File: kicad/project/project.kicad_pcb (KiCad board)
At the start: 2 copper layers, 98 x 60 mm, 49 parts, among them J1 SWD, J3 Voltmeter, U1 ADS1015, U2 AP7380, U3 STM32L031F4Px, U4 VN7003ALH

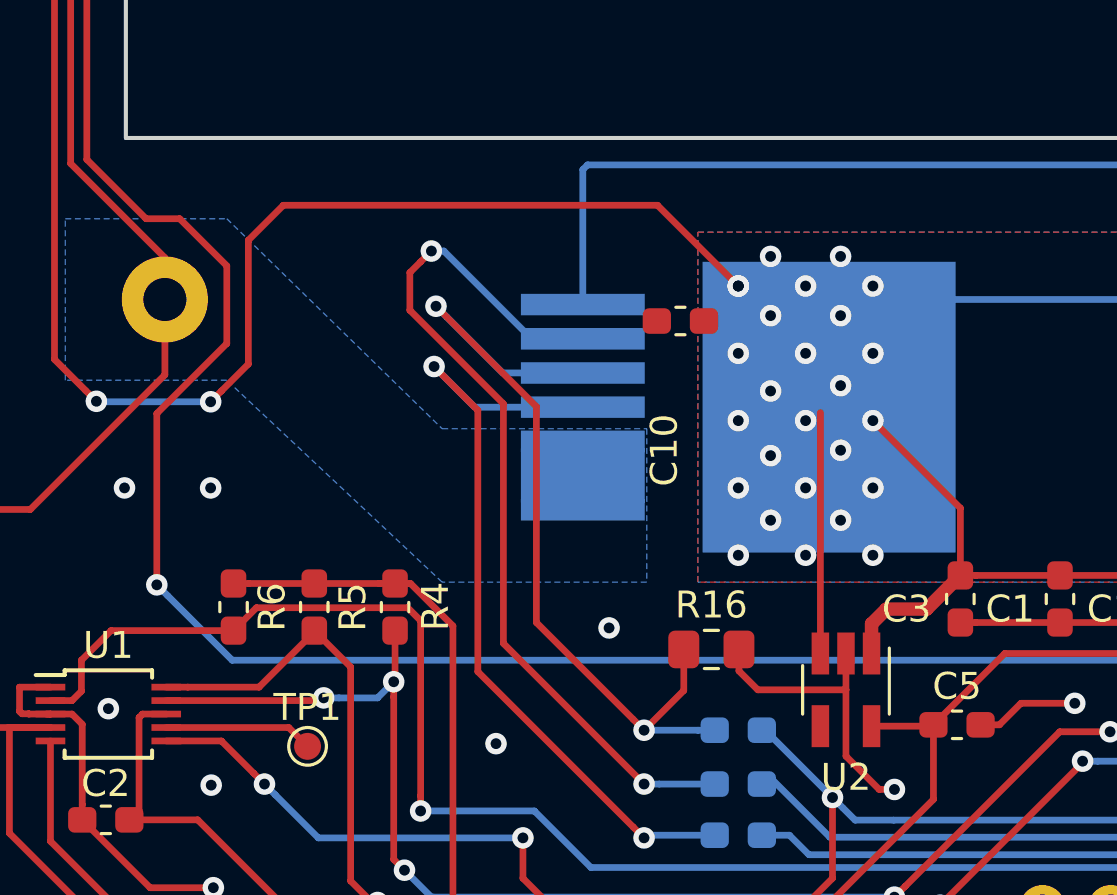
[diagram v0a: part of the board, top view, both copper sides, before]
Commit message: Corrected octopak footprint
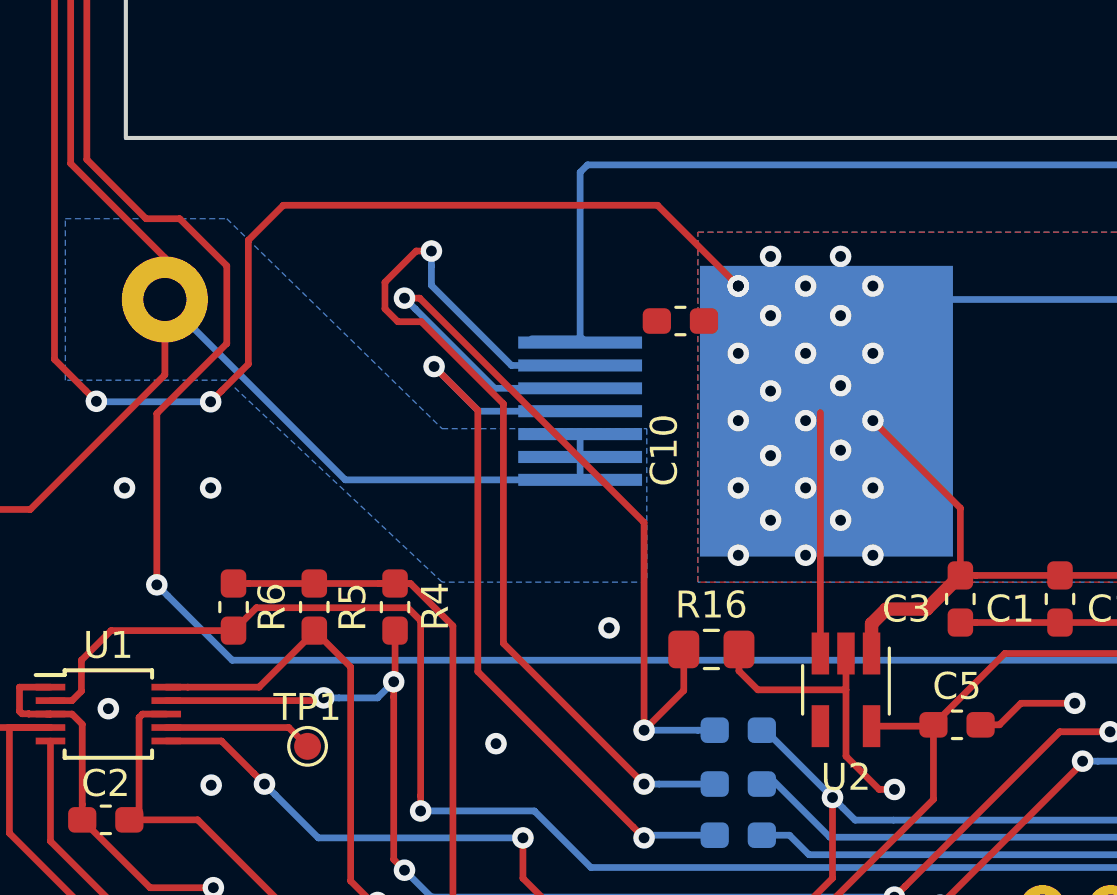
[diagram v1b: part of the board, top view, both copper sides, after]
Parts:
- moved U4 0.18 mm to (137.4, 112.2)
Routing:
- net /OUT: track 61.2 -> 81.1 mm
- net GND: track 178.3 -> 181.7 mm
- net /FR_DIAG: track 33.6 -> 36.2 mm
- net Net-(R13-Pad1): track 31.7 -> 34.2 mm

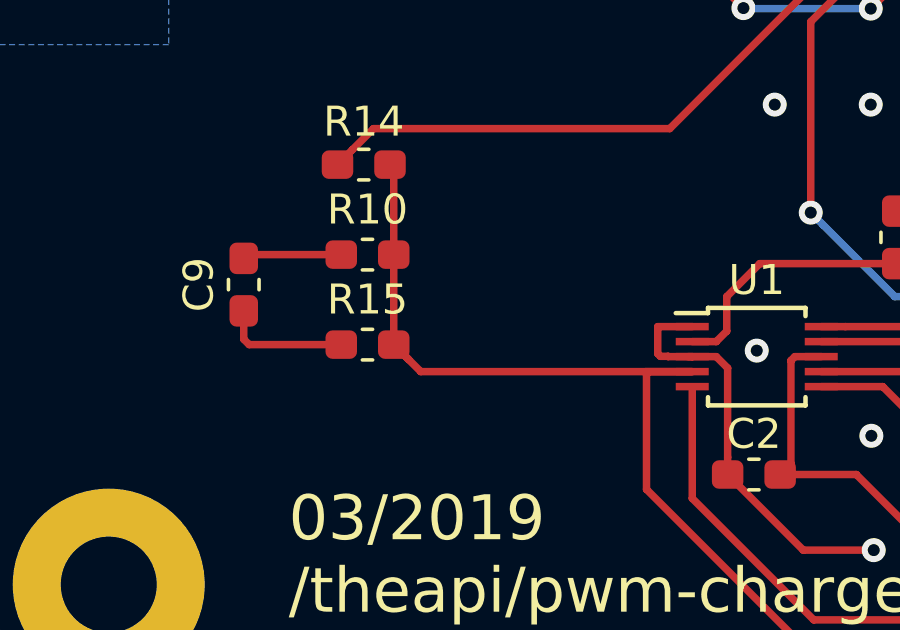
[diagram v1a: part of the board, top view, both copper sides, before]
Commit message: BATT_SENSE RC filter fix
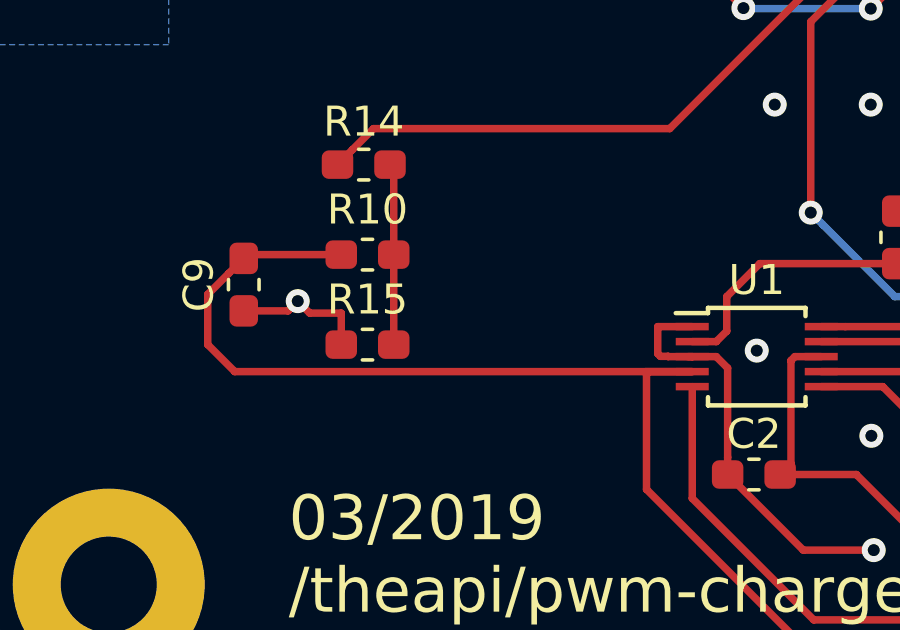
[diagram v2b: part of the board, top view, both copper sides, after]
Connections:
- C9 pad 1: Net-(C9-Pad1) -> /BATT_SENSE
- R10 pad 1: /BATT_SENSE -> Net-(R10-Pad1)
- R10 pad 2: Net-(C9-Pad1) -> /BATT_SENSE
- R14 pad 2: /BATT_SENSE -> Net-(R10-Pad1)
- R15 pad 1: /BATT_SENSE -> Net-(R10-Pad1)
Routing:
- net /BATT_SENSE: track 96.4 -> 102.5 mm
- net Net-(R10-Pad1): track 0.00 -> 6.05 mm
- net Net-(C9-Pad1): track 3.30 -> 0.00 mm
- net GND: track 181.7 -> 182.0 mm, vias 12 -> 13

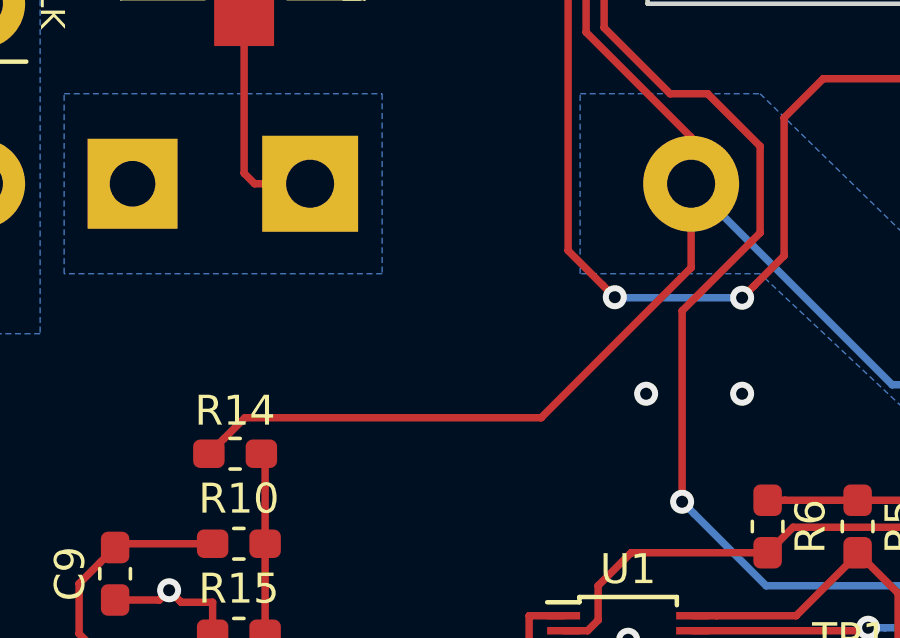
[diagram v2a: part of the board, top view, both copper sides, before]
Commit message: Measure after the diode to get the battery voltage
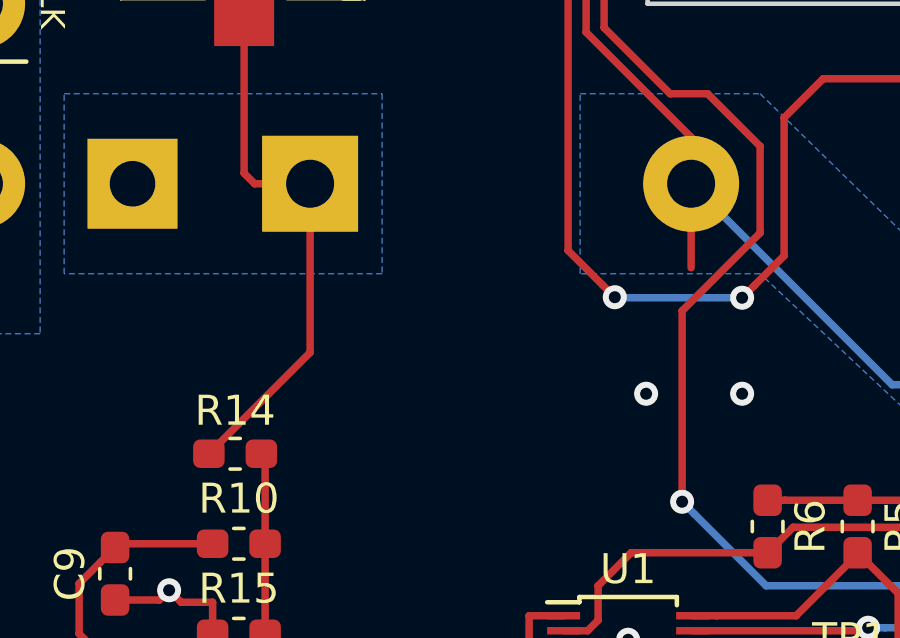
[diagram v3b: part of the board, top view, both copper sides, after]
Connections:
- R14 pad 1: /OUT -> /DIODE
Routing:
- net /OUT: track 81.1 -> 62.4 mm
- net /DIODE: track 7.84 -> 18.2 mm
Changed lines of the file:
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@@
     (thickness 1.6)
     (drawings 45)
-    (tracks 495)
+    (tracks 493)
     (zones 0)
     (modules 49)
@@
     )
     (pad 1 smd roundrect (at -0.875 0) (size 1.05 0.95) (layers F.Cu F.Paste F.Mask) (roundrect_rratio 0.25)
-      (net 31 /OUT))
+      (net 32 /DIODE))
     (pad 2 smd roundrect (at 0.875 0) (size 1.05 0.95) (layers F.Cu F.Paste F.Mask) (roundrect_rratio 0.25)
       (net 33 "Net-(R10-Pad1)"))
@@
   (segment (start 115.9 112.236411) (end 118.5 109.636411) (width 0.25) (layer F.Cu) (net 30))
   (segment (start 118.5 106.75) (end 116.75 105) (width 0.25) (layer F.Cu) (net 30))
-  (segment (start 100.624072 116.500928) (end 100.125 117) (width 0.25) (layer F.Cu) (net 31))
   (segment (start 116.2 108) (end 116.2 110.8) (width 0.25) (layer F.Cu) (net 31))
-  (segment (start 101.325 115.8) (end 100.624072 116.500928) (width 0.25) (layer F.Cu) (net 31))
-  (segment (start 116.2 110.8) (end 111.2 115.8) (width 0.25) (layer F.Cu) (net 31))
-  (segment (start 111.2 115.8) (end 101.325 115.8) (width 0.25) (layer F.Cu) (net 31))
   (segment (start 106.475 85) (end 100.074072 91.400928) (width 0.25) (layer F.Cu) (net 31))
   (segment (start 111.5 85) (end 106.475 85) (width 0.25) (layer F.Cu) (net 31))
@@
   (segment (start 101.3 107.65) (end 101.65 108) (width 0.25) (layer F.Cu) (net 32))
   (segment (start 101.3 102.155) (end 101.3 107.65) (width 0.25) (layer F.Cu) (net 32))
+  (segment (start 103.5 113.625) (end 103.5 108) (width 0.25) (layer F.Cu) (net 32))
+  (segment (start 100.125 117) (end 103.5 113.625) (width 0.25) (layer F.Cu) (net 32))
   (zone (net 2) (net_name +24V) (layer B.Cu) (hatch edge 0.508)
     (priority 10)

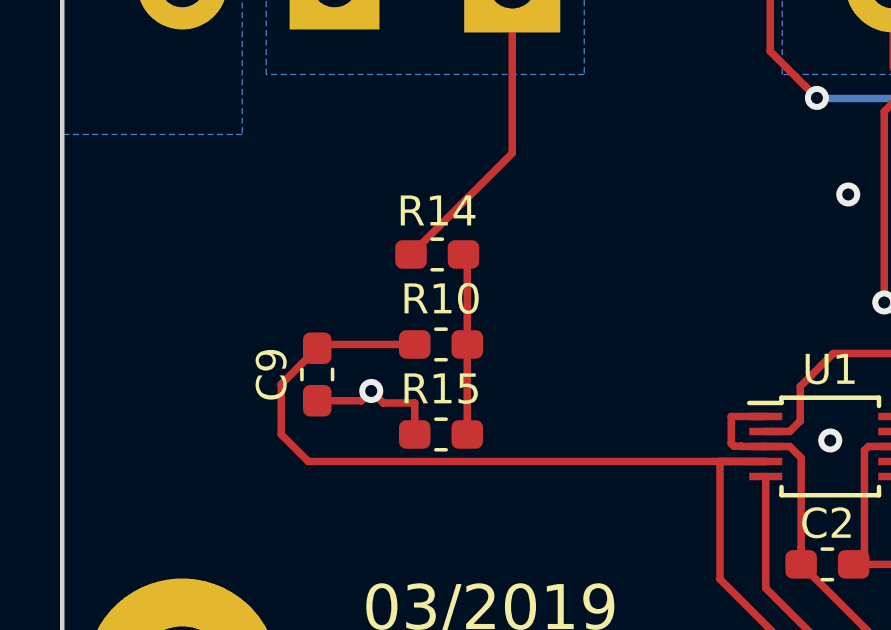
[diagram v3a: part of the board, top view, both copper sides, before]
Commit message: Removed extra resistor
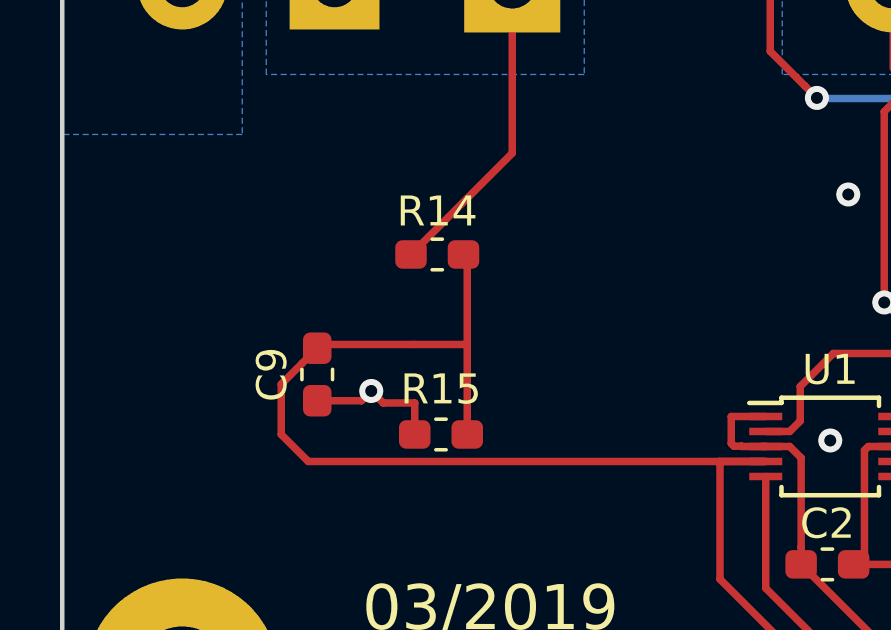
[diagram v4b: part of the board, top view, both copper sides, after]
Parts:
- removed R10: 10K, Resistor_SMD:R_0603_1608Metric_Pad1.05x0.95mm_HandSolder
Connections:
- R14 pad 2: Net-(R10-Pad1) -> /BATT_SENSE
- R15 pad 1: Net-(R10-Pad1) -> /BATT_SENSE
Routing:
- net /BATT_SENSE: track 102.5 -> 110.3 mm
- net Net-(R10-Pad1): track 6.05 -> 0.00 mm
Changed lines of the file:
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@@
     (thickness 1.6)
     (drawings 45)
-    (tracks 493)
+    (tracks 494)
     (zones 0)
-    (modules 49)
-    (nets 34)
+    (modules 48)
+    (nets 33)
   )
   (page A4)
@@
   (net 31 /OUT)
   (net 32 /DIODE)
-  (net 33 "Net-(R10-Pad1)")
   (net_class Default "This is the default net class."
     (clearance 0.2)
@@
     (add_net "Net-(D2-Pad2)")
     (add_net "Net-(D3-Pad2)")
-    (add_net "Net-(R10-Pad1)")
     (add_net "Net-(R12-Pad2)")
     (add_net "Net-(R13-Pad1)")
@@
     )
   )
-  (module Resistor_SMD:R_0603_1608Metric_Pad1.05x0.95mm_HandSolder (layer F.Cu)
-    (at 101.125 120 180)
-    (descr "Resistor SMD 0603 (1608 Metric), square (rectangular) end terminal, IPC_7351 nominal with elongated pad for handsoldering. (Body size source: http://www.tortai-tech.com/upload/download/2011102023233369053.pdf), generated with kicad-footprint-generator")
-    (tags "resistor handsolder")
-    (attr smd)
-    (fp_text reference R10 (at 0 1.5 180) (layer F.SilkS)
-      (effects (font (size 1 1) (thickness 0.15)))
-    )
-    (fp_text value 10K (at -3.25 0 180) (layer F.Fab)
-      (effects (font (size 1 1) (thickness 0.15)))
-    )
-    (fp_text user %R (at 0 0 180) (layer F.Fab)
-      (effects (font (size 0.4 0.4) (thickness 0.06)))
-    )
-    (fp_line (start 1.65 0.73) (end -1.65 0.73) (layer F.CrtYd) (width 0.05))
-    (fp_line (start 1.65 -0.73) (end 1.65 0.73) (layer F.CrtYd) (width 0.05))
-    (fp_line (start -1.65 -0.73) (end 1.65 -0.73) (layer F.CrtYd) (width 0.05))
-    (fp_line (start -1.65 0.73) (end -1.65 -0.73) (layer F.CrtYd) (width 0.05))
-    (fp_line (start -0.171267 0.51) (end 0.171267 0.51) (layer F.SilkS) (width 0.12))
-    (fp_line (start -0.171267 -0.51) (end 0.171267 -0.51) (layer F.SilkS) (width 0.12))
-    (fp_line (start 0.8 0.4) (end -0.8 0.4) (layer F.Fab) (width 0.1))
-    (fp_line (start 0.8 -0.4) (end 0.8 0.4) (layer F.Fab) (width 0.1))
-    (fp_line (start -0.8 -0.4) (end 0.8 -0.4) (layer F.Fab) (width 0.1))
-    (fp_line (start -0.8 0.4) (end -0.8 -0.4) (layer F.Fab) (width 0.1))
-    (pad 2 smd roundrect (at 0.875 0 180) (size 1.05 0.95) (layers F.Cu F.Paste F.Mask) (roundrect_rratio 0.25)
-      (net 16 /BATT_SENSE))
-    (pad 1 smd roundrect (at -0.875 0 180) (size 1.05 0.95) (layers F.Cu F.Paste F.Mask) (roundrect_rratio 0.25)
-      (net 33 "Net-(R10-Pad1)"))
-    (model ${KISYS3DMOD}/Resistor_SMD.3dshapes/R_0603_1608Metric.wrl
-      (at (xyz 0 0 0))
-      (scale (xyz 1 1 1))
-      (rotate (xyz 0 0 0))
-    )
-  )
   (module Resistor_SMD:R_0603_1608Metric_Pad1.05x0.95mm_HandSolder (layer B.Cu)
     (at 137.5 127.9)
@@
       (net 32 /DIODE))
     (pad 2 smd roundrect (at 0.875 0) (size 1.05 0.95) (layers F.Cu F.Paste F.Mask) (roundrect_rratio 0.25)
-      (net 33 "Net-(R10-Pad1)"))
+      (net 16 /BATT_SENSE))
     (model ${KISYS3DMOD}/Resistor_SMD.3dshapes/R_0603_1608Metric.wrl
       (at (xyz 0 0 0))
@@
       (net 1 GND))
     (pad 1 smd roundrect (at -0.875 0 180) (size 1.05 0.95) (layers F.Cu F.Paste F.Mask) (roundrect_rratio 0.25)
-      (net 33 "Net-(R10-Pad1)"))
+      (net 16 /BATT_SENSE))
     (model ${KISYS3DMOD}/Resistor_SMD.3dshapes/R_0603_1608Metric.wrl
       (at (xyz 0 0 0))
@@
   (segment (start 160.2 121.15) (end 160.8 121.75) (width 0.25) (layer F.Cu) (net 3))
   (segment (start 144.75 123.8) (end 147.4 121.15) (width 0.25) (layer F.Cu) (net 3))
-  (segment (start 97.125 120) (end 97 120.125) (width 0.25) (layer F.Cu) (net 16))
-  (segment (start 100.25 120) (end 97.125 120) (width 0.25) (layer F.Cu) (net 16))
   (via (at 177.39 85.91) (size 0.8) (drill 0.4) (layers F.Cu B.Cu) (net 4))
   (segment (start 175.265 85.91) (end 177.39 85.91) (width 0.25) (layer F.Cu) (net 4))
@@
   (segment (start 178.41 127.29) (end 182.725002 122.974998) (width 0.25) (layer F.Cu) (net 15))
   (segment (start 182.725002 115.940002) (end 180.854072 114.069072) (width 0.25) (layer F.Cu) (net 15))
+  (segment (start 97.125 120) (end 97 120.125) (width 0.25) (layer F.Cu) (net 16))
+  (segment (start 100.25 120) (end 97.125 120) (width 0.25) (layer F.Cu) (net 16))
   (segment (start 172.55 126.675) (end 173.955 126.675) (width 0.25) (layer B.Cu) (net 16))
   (segment (start 173.955 126.675) (end 176.09 128.81) (width 0.25) (layer B.Cu) (net 16))
   (via (at 176.09 128.81) (size 0.8) (drill 0.4) (layers F.Cu B.Cu) (net 16))
-  (segment (start 102 123) (end 102 120) (width 0.25) (layer F.Cu) (net 33))
-  (segment (start 102 117.125) (end 101.875 117) (width 0.25) (layer F.Cu) (net 33))
-  (segment (start 102 120) (end 102 117.125) (width 0.25) (layer F.Cu) (net 33))
   (segment (start 175.524315 128.81) (end 176.09 128.81) (width 0.25) (layer F.Cu) (net 16))
   (segment (start 171.534315 132.8) (end 175.524315 128.81) (width 0.25) (layer F.Cu) (net 16))
@@
   (segment (start 103.5 113.625) (end 103.5 108) (width 0.25) (layer F.Cu) (net 32))
   (segment (start 100.125 117) (end 103.5 113.625) (width 0.25) (layer F.Cu) (net 32))
+  (segment (start 102 123) (end 102 120) (width 0.25) (layer F.Cu) (net 16))
+  (segment (start 102 117.125) (end 101.875 117) (width 0.25) (layer F.Cu) (net 16))
+  (segment (start 102 120) (end 102 117.125) (width 0.25) (layer F.Cu) (net 16))
+  (segment (start 100.25 120) (end 102 120) (width 0.25) (layer F.Cu) (net 16))
   (zone (net 2) (net_name +24V) (layer B.Cu) (hatch edge 0.508)
     (priority 10)
